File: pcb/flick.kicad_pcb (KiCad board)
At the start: 2 copper layers, 100 x 60 mm, 42 parts, among them J1 DEBUG, Q1 Q_Photo_NPN, Q2 Q_NMOS_GSD, SW1 Rotary_Encoder_Switch, SW2 RESET, U1 ATSAMD21G18A-AFT, U2 AP2112M-3.3, X1 USB_C_2.0, X2 SH1106G, Y1 32.768KHz

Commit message: initial 100x60 version where I think everything works
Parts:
- moved C4 2.30 mm to (119.9, 63.8)
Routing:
- net /VBUS_RAW: track 15.7 -> 43.7 mm, vias 2 -> 0
- net +3.3VA: track 88.8 -> 82.3 mm
- net GND: track 34.1 -> 30.3 mm
- net +3V3: track 143.7 -> 143.4 mm, vias 8 -> 7

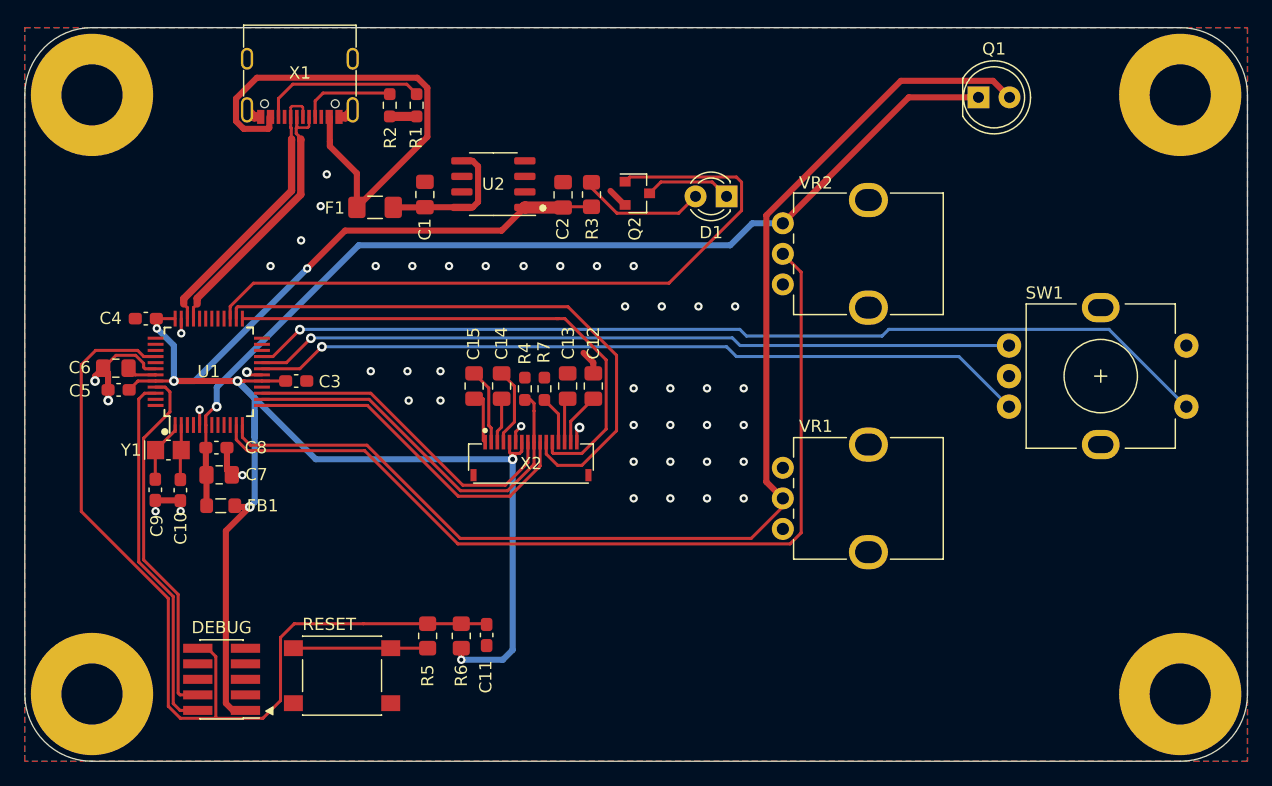
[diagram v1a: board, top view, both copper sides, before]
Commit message: Shrink to 95x50mm part 1
Mostly done with the routing, but there's still some power traces to
figure out, as well as deciding what to do with various local ground
planes (moar via stitching probably).

  * Mostly the same layout but smaller overall (to save cost at OSHPark
    which charges per square inch).
  * Remove LED driver Q2 because 7mA is actually plenty to drive an LED
    directly from the SAMD21.
  * Replace AP2112M with AP7365 voltage regulator in an SOT-25 package
    rather than chonky SOIC-8
  * Use surface mount headers for SWD debug rather than through-hole;
    makes routing slightly easier.
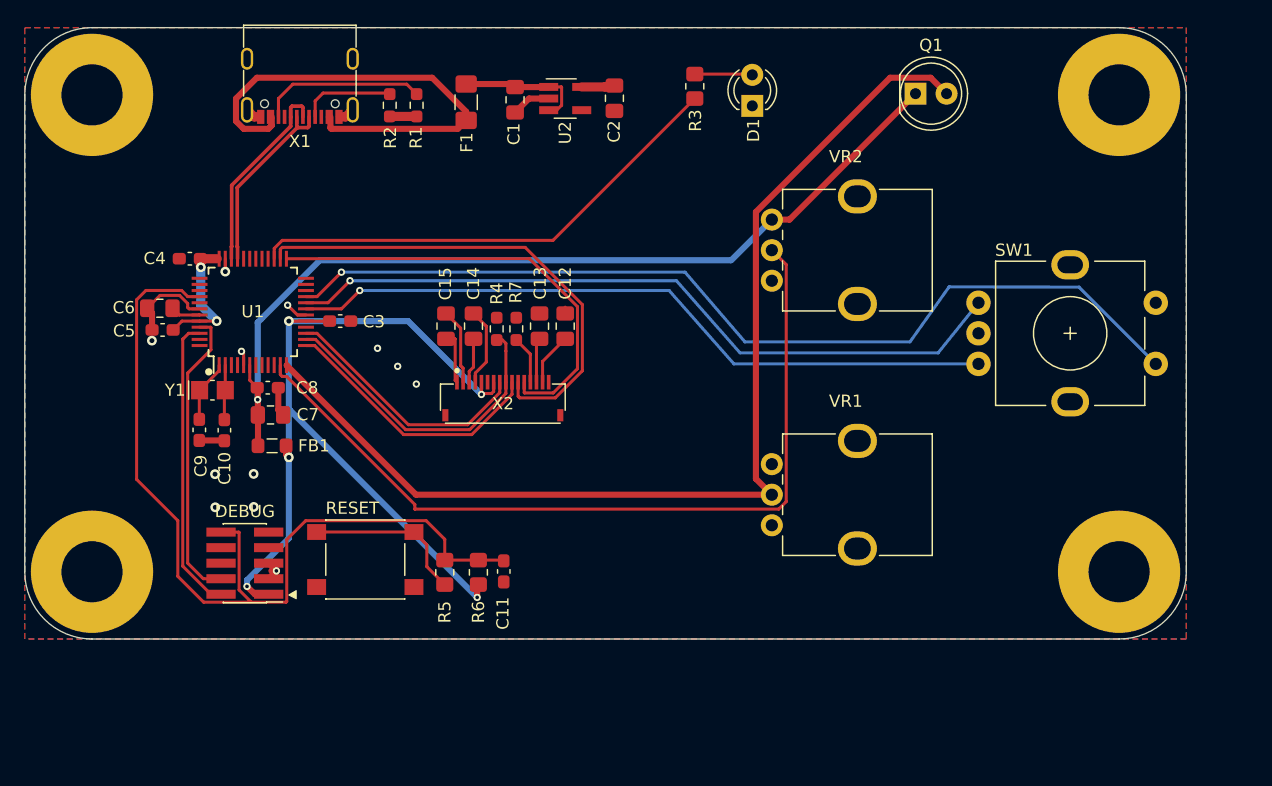
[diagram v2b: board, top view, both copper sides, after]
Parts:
- removed Q2: Q_NMOS_GSD, Package_TO_SOT_SMD:SOT-23
- REF**: footprint Alkenta:SH1106G_SCREEN -> Wild:SH1106G_SCREEN
- U2: value AP2112M-3.3 -> AP7365-33W; footprint Package_SO:SO-8_3.9x4.9mm_P1.27mm -> Package_TO_SOT_SMD:SOT-23-5_HandSoldering
- VR1, VR2: footprint Alkenta:Potentiometer_Bourns_PTV09A-1_Single_Vertical -> Wild:Potentiometer_Bourns_PTV09A-1_Single_Vertical
- X1: footprint Alkenta:USB_C_Receptacle_GCT_USB4105 -> Wild:USB_C_Receptacle_GCT_USB4105
- X2: footprint Alkenta:GCT_FFC2B28-16_1x16-1MP_P0.5mm_Horizontal -> Wild:GCT_FFC2B28-16_1x16-1MP_P0.5mm_Horizontal
- moved R3 12.2 mm to (164.8, 44.8)
- moved F1 11.4 mm to (146.1, 46.1), turned to 270 degrees
- moved H4 11.2 mm to (199.5, 84.5)
- moved C1 10.7 mm to (150.1, 45.9), turned to 270 degrees
- moved H3 10.0 mm to (115.5, 84.5)
- moved J1 9.69 mm to (128.0, 83.8)
- moved SW2 9.69 mm to (137.8, 83.5)
- moved U2 9.14 mm to (154.2, 45.8), turned to 0 degrees
- moved C2 8.95 mm to (158.2, 45.8), turned to 270 degrees
- moved D1 7.69 mm to (169.5, 46.4), turned to 90 degrees
- moved C7 6.45 mm to (130.1, 71.7)
- moved C8 6.45 mm to (129.9, 69.5)
- moved FB1 6.45 mm to (130.2, 74.2)
- moved C3 6.08 mm to (135.8, 64.0)
- moved C10 6.08 mm to (126.3, 72.9)
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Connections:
- D1 pad 1: Net-(D1-Pad1) -> GND
- R3 pad 1: +3V3 -> LED_TRIG
- U2 pad 1: +3V3 -> +5V
- U2 pad 2: (no net) -> GND
- U2 pad 3: (no net) -> +5V
- U2 pad 5: +5V -> +3V3
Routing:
- net +3V3: track 143.4 -> 87.2 mm
- net LED_TRIG: track 58.2 -> 40.3 mm
- net PHOTO_VAL: track 99.1 -> 88.4 mm
- net OLED_SCK: track 48.1 -> 40.3 mm
- net USB_D-: track 22.9 -> 15.3 mm
- net +3.3VA: track 82.3 -> 74.8 mm
- net Net-(D1-Pad1): track 7.17 -> 0.00 mm
- net USB_D+: track 22.9 -> 16.3 mm
- net OLED_DC: track 28.8 -> 22.2 mm
- net OLED_MOSI: track 43.1 -> 36.5 mm
- net PHOTO_THRESH: track 74.7 -> 68.2 mm
- net OLED_RESET: track 32.1 -> 25.6 mm
- net OLED_CS: track 27.3 -> 20.9 mm
- net SWDIO: track 29.9 -> 24.2 mm
- net Net-(D1-Pad2): track 10.4 -> 4.72 mm
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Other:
- board size 100 x 60 mm -> 95 x 50 mm
- net class Default: via_dia 0.6858 -> 0.6; via_drill 0.3302 -> 0.3

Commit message: draft of v1 shrink complete
Add test points, flip the phototransistor footprint around (so
anode/cathode is consistent with standard LEDs), finish routing power
and stuff.

TODO: Add silkscreen text/graphics, verify I can actually order
everything in the BOM, double-check everything before production.
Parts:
- added TP1: GND, Wild:TestPoint_THTPad_D1.6mm_Drill1.0mm, F.Cu at (162.0, 43.5)
- added TP2: VCC, Wild:TestPoint_THTPad_D1.6mm_Drill1.0mm, F.Cu at (167.1, 43.5)
- added TP3: VCCA, Wild:TestPoint_THTPad_D1.6mm_Drill1.0mm, F.Cu at (172.1, 43.5)
- added TP4: THRSH, Wild:TestPoint_THTPad_D1.6mm_Drill1.0mm, F.Cu at (177.2, 43.5)
- added TP5: VAL, Wild:TestPoint_THTPad_D1.6mm_Drill1.0mm, F.Cu at (182.3, 43.5)
- moved Q1 8.26 mm to (191.1, 45.8), turned to 180 degrees
- moved R3 4.61 mm to (162.2, 48.6)
- moved D1 3.23 mm to (166.5, 47.6), turned to 270 degrees
- moved C4 1.72 mm to (124.0, 57.2)
- moved C11 0.55 mm to (148.7, 84.3)
- moved R6 0.45 mm to (146.7, 84.5)
- moved C3 0.27 mm to (135.7, 64.2)
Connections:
- J1 pad 6: (no net) -> Net-(J1-Pad6)
- J1 pad 7: (no net) -> Net-(J1-Pad7)
- J1 pad 8: (no net) -> Net-(J1-Pad8)
- J1 pad 9: (no net) -> Net-(J1-Pad9)
- Q1 pad 1: +3.3VA -> PHOTO_VAL
- Q1 pad 2: PHOTO_VAL -> +3.3VA
- U1 pad 10: (no net) -> Net-(U1-Pad10)
- U1 pad 16: (no net) -> Net-(U1-Pad16)
- U1 pad 22: (no net) -> Net-(U1-Pad22)
- U1 pad 23: (no net) -> Net-(U1-Pad23)
- U1 pad 24: (no net) -> Net-(U1-Pad24)
- U1 pad 28: (no net) -> Net-(U1-Pad28)
- U1 pad 29: (no net) -> Net-(U1-Pad29)
- U1 pad 3: (no net) -> Net-(U1-Pad3)
- U1 pad 30: (no net) -> Net-(U1-Pad30)
- U1 pad 31: (no net) -> Net-(U1-Pad31)
- U1 pad 32: (no net) -> Net-(U1-Pad32)
- U1 pad 37: (no net) -> Net-(U1-Pad37)
- U1 pad 38: (no net) -> Net-(U1-Pad38)
- U1 pad 39: (no net) -> Net-(U1-Pad39)
- U1 pad 4: (no net) -> Net-(U1-Pad4)
- U1 pad 41: (no net) -> Net-(U1-Pad41)
- U1 pad 47: (no net) -> Net-(U1-Pad47)
- U1 pad 48: (no net) -> Net-(U1-Pad48)
- U1 pad 7: (no net) -> Net-(U1-Pad7)
- U1 pad 8: (no net) -> Net-(U1-Pad8)
- U1 pad 9: (no net) -> Net-(U1-Pad9)
- U2 pad 4: (no net) -> Net-(U2-Pad4)
- VR1 pad 3: (no net) -> Net-(VR1-Pad3)
- X1 pad A8: (no net) -> Net-(X1-PadA8)
- X1 pad B8: (no net) -> Net-(X1-PadB8)
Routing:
- net +3V3: track 87.2 -> 166.7 mm
- net +3.3VA: track 74.8 -> 116.5 mm, vias 1 -> 2
- net PHOTO_THRESH: track 68.2 -> 85.2 mm
- net GND: track 27.0 -> 38.9 mm, vias 12 -> 59
- net PHOTO_VAL: track 88.4 -> 99.1 mm
- net LED_TRIG: track 40.3 -> 36.1 mm
- net USB_D-: track 15.3 -> 16.3 mm
- net Net-(D1-Pad2): track 4.72 -> 5.46 mm

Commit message: Flick v1 PCB Rev A Final
Here we go, I'm gonna send this to OSH Park and hope it works. Minor
layout tweaks, add silkscreen decorations, and double-check everything.
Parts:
- removed REF**: SH1106G_SCREEN, Wild:SH1106G_SCREEN
- added G***: LOGO, Wild:PoomFace, B.Cu at (195.1, 65.1)
- added G***: LOGO, Wild:NyanCatLOL, B.Cu at (135.2, 57.5)
- added X3: SH1106G_Screen, Wild:SH1106G_SCREEN, F.Cu at (149.1, 65.0)
- added svg2mod: G***, Wild:Logo_OSHW_Text_7mm, F.Cu at (187.1, 81.5)
- FB1: value 50ohm @ 20MHz -> 220ohm @ 100MHz
- SW1: footprint Alkenta:RotaryEncoder_Bourns_PEC11L-Switch_Vertical_H20mm -> Wild:RotaryEncoder_Bourns_PEC11L-Switch_Vertical_H20mm
- U1: value ATSAMD21G18A-AFT -> ATSAMD21G18A-A
- moved Q1 2.05 mm to (190.7, 43.8)
- moved FB1 0.96 mm to (129.7, 73.4), turned to 180 degrees
- moved C7 0.53 mm to (129.7, 71.4), turned to 180 degrees
- moved C8 0.48 mm to (129.4, 69.5), turned to 180 degrees
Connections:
- J1 pad 6: Net-(J1-Pad6) -> (no net)
- J1 pad 7: Net-(J1-Pad7) -> (no net)
- J1 pad 8: Net-(J1-Pad8) -> (no net)
- J1 pad 9: Net-(J1-Pad9) -> (no net)
- U1 pad 10: Net-(U1-Pad10) -> (no net)
- U1 pad 16: Net-(U1-Pad16) -> (no net)
- U1 pad 22: Net-(U1-Pad22) -> (no net)
- U1 pad 23: Net-(U1-Pad23) -> (no net)
- U1 pad 24: Net-(U1-Pad24) -> (no net)
- U1 pad 28: Net-(U1-Pad28) -> (no net)
- U1 pad 29: Net-(U1-Pad29) -> (no net)
- U1 pad 3: Net-(U1-Pad3) -> (no net)
- U1 pad 30: Net-(U1-Pad30) -> (no net)
- U1 pad 31: Net-(U1-Pad31) -> (no net)
- U1 pad 32: Net-(U1-Pad32) -> (no net)
- U1 pad 37: Net-(U1-Pad37) -> (no net)
- U1 pad 38: Net-(U1-Pad38) -> (no net)
- U1 pad 39: Net-(U1-Pad39) -> (no net)
- U1 pad 4: Net-(U1-Pad4) -> (no net)
- U1 pad 41: Net-(U1-Pad41) -> (no net)
- U1 pad 47: Net-(U1-Pad47) -> (no net)
- U1 pad 48: Net-(U1-Pad48) -> (no net)
- U1 pad 7: Net-(U1-Pad7) -> (no net)
- U1 pad 8: Net-(U1-Pad8) -> (no net)
- U1 pad 9: Net-(U1-Pad9) -> (no net)
- U2 pad 4: Net-(U2-Pad4) -> (no net)
- VR1 pad 3: Net-(VR1-Pad3) -> (no net)
- X1 pad A8: Net-(X1-PadA8) -> (no net)
- X1 pad B8: Net-(X1-PadB8) -> (no net)
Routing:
- net SWCLK: track 24.2 -> 28.0 mm
- net SWDIO: track 24.2 -> 26.9 mm
- net +3.3VA: track 116.5 -> 115.3 mm, vias 2 -> 0
- net PHOTO_VAL: track 99.1 -> 98.5 mm
- net GND: track 38.9 -> 38.6 mm, vias 59 -> 55
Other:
- board text added: "Flick!"
- board text added: "Rev A 11/2021"
- board text added: "Top Mid!"
